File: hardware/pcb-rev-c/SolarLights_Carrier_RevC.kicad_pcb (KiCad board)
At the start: 2 copper layers, 74 x 51.5 mm, 30 parts, among them M1 TP4056 module, Q2 2N3904 / EBC

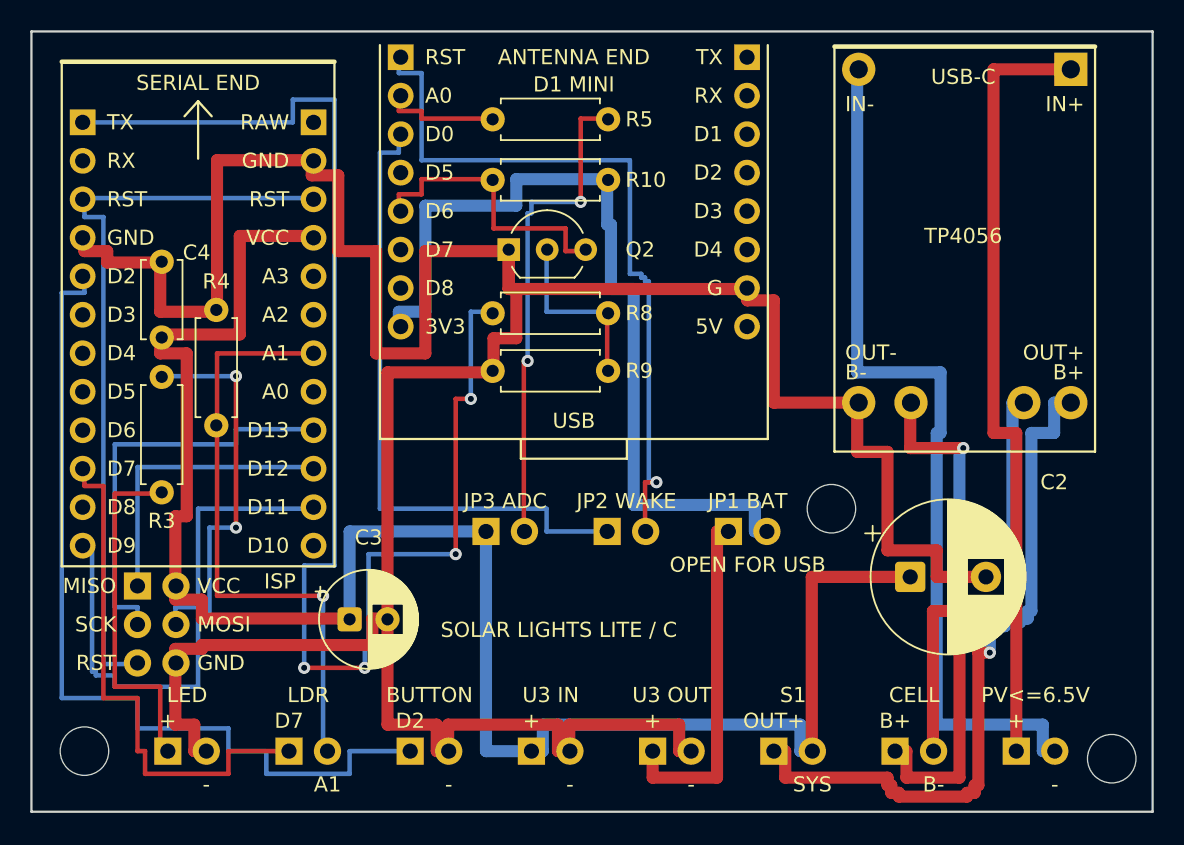
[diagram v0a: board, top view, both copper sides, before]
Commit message: feat(pcb): carrier Rev C with LDR trim, TEST button and box-header ISP
R3 56R, R4 22k + RV1 50k 3296W rheostat, on-board 6x6 TEST switch, sideways
ISP with optional DC3-6P box header, name and repo on silkscreen. Docs 01-13,
drawings, layouts, netlist, KiCad schematic and renders follow Rev C.
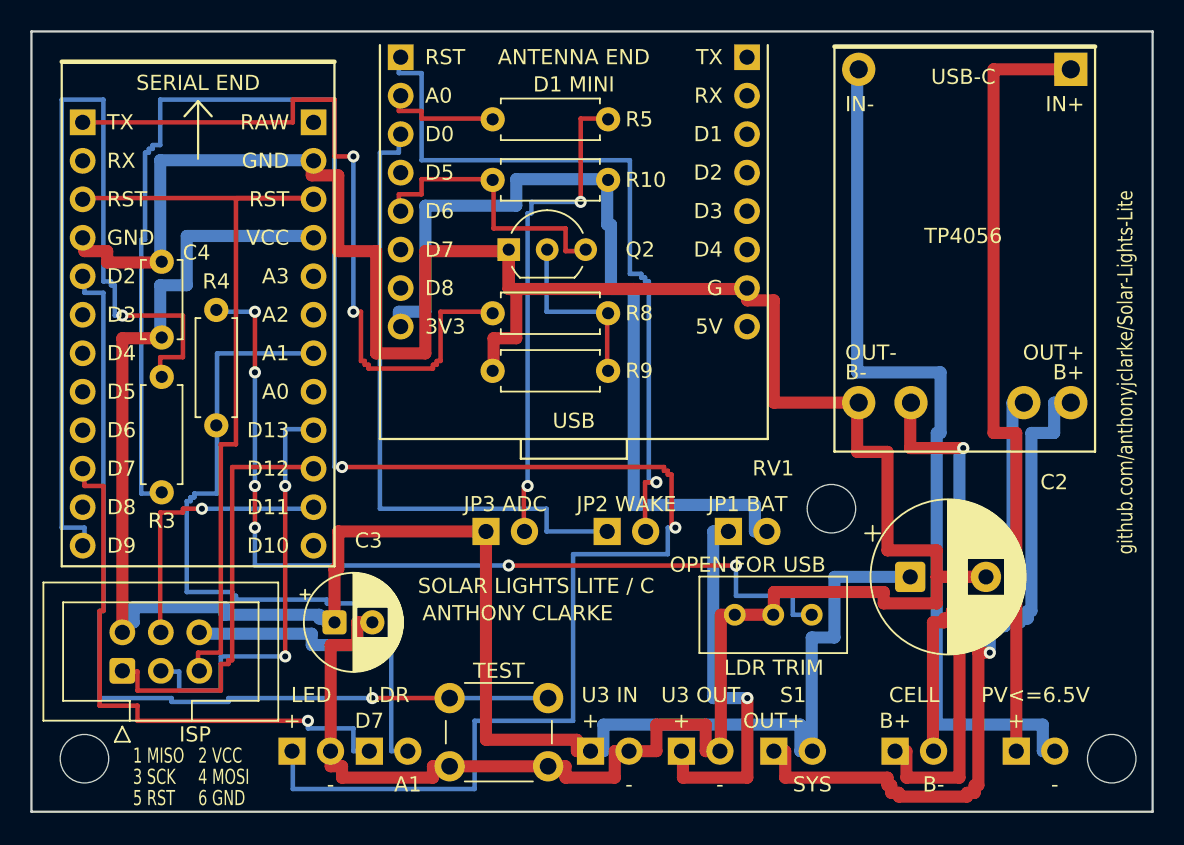
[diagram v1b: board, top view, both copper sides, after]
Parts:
- removed JBUTTON1: SW1 D2 / -, Carrier:SolderPads_1x02_P2.54mm
- added RV1: 50k 3296W, Carrier:Potentiometer_Bourns_3296W_Vertical, F.Cu at (101.5, 88.5)
- added SW1: 6x6 tactile, Carrier:SW_PUSH_6mm_H9.5mm, F.Cu at (77.6, 94.0)
- JISP1: value ISP -> 2x3 male header 2.54 mm; footprint Carrier:Pads_2x03_P2.54mm -> Carrier:IDC-Header_2x03_P2.54mm_Vertical
- R3: value 47R / 0.25W -> 56R / 0.25W
- R4: value 47k -> 22k
- moved JLED1 8.20 mm to (67.2, 97.5)
- moved JISP1 5.69 mm to (56.0, 92.2), turned to 90 degrees
- moved JLDR1 5.30 mm to (72.3, 97.5)
- moved JU3IN1 3.90 mm to (86.9, 97.5)
- moved JU3OUT1 1.90 mm to (92.9, 97.5)
- moved C3 1.02 mm to (70.0, 89.0)
- moved H1 0.50 mm to (53.5, 98.0)
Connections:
- R4 pad 2: /GND_LOAD -> /LDR_TRIM
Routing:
- net /LED_POS: track 23.6 -> 135.9 mm, vias 0 -> 2
- net /LDR_TRIM: track 0.00 -> 59.4 mm, vias 0 -> 6
- net /UART_TX: track 93.7 -> 50.2 mm, vias 4 -> 2
- net /PWM: track 45.0 -> 59.0 mm, vias 2 -> 1
- net /LDR_SENSE: track 40.0 -> 49.3 mm, vias 1 -> 0
- net /ISP_MISO: track 19.5 -> 28.7 mm
- net /VBAT_SYS: track 122.3 -> 129.9 mm
- net /AVR_RESET: track 49.8 -> 54.3 mm
- net /LDR_POWER: track 35.4 -> 38.2 mm, vias 0 -> 1
- net /REG_3V3: track 23.0 -> 25.6 mm, vias 0 -> 1
- net /ISP_MOSI: track 17.0 -> 18.5 mm, vias 0 -> 1
- net /ISP_SCK: track 27.7 -> 28.7 mm, vias 0 -> 2
- net /TEST: track 58.9 -> 59.7 mm, vias 0 -> 1
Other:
- board text added: "1 MISO"
- board text added: "2 VCC"
- board text added: "3 SCK"
- board text added: "4 MOSI"
- board text added: "5 RST"
- board text added: "6 GND"
- board text added: "ANTHONY CLARKE"
- board text added: "LDR TRIM"
- board text added: "TEST"
- board text added: "github.com/anthonyjclarke/Solar-Lights-Lite"
- board text removed: "BUTTON"
- board text removed: "MISO"
- board text removed: "MOSI"
- board text removed: "SCK"
